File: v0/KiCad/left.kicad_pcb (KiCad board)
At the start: 2 copper layers, 153.3 x 124.9 mm, 3 parts

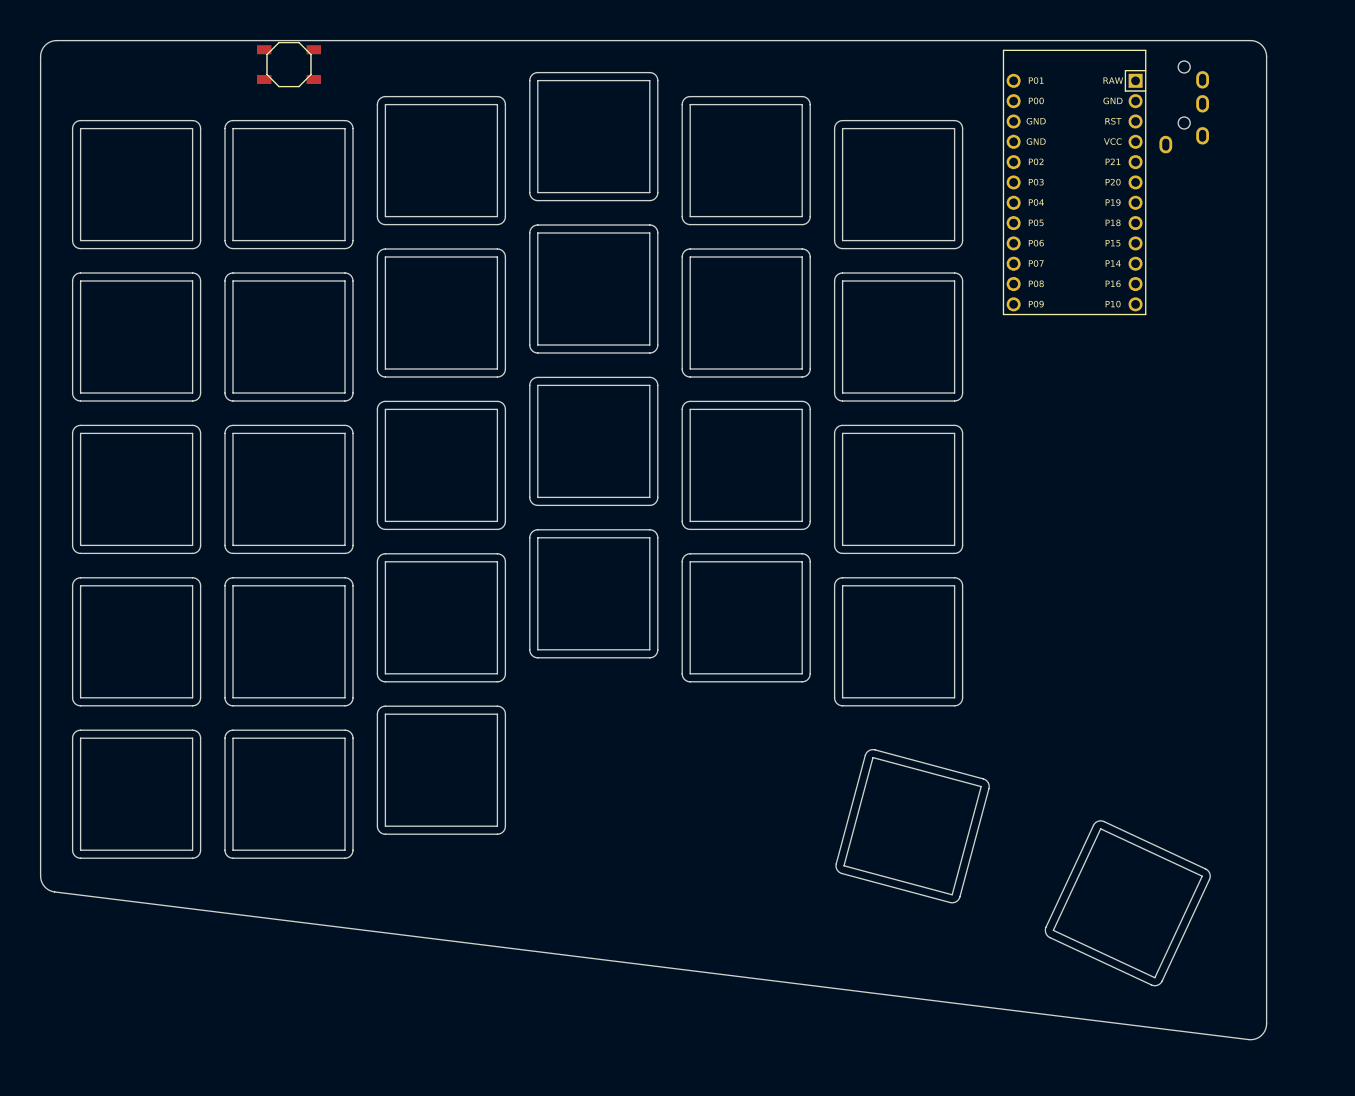
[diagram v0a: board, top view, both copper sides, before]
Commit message: Use 1.5u for mod
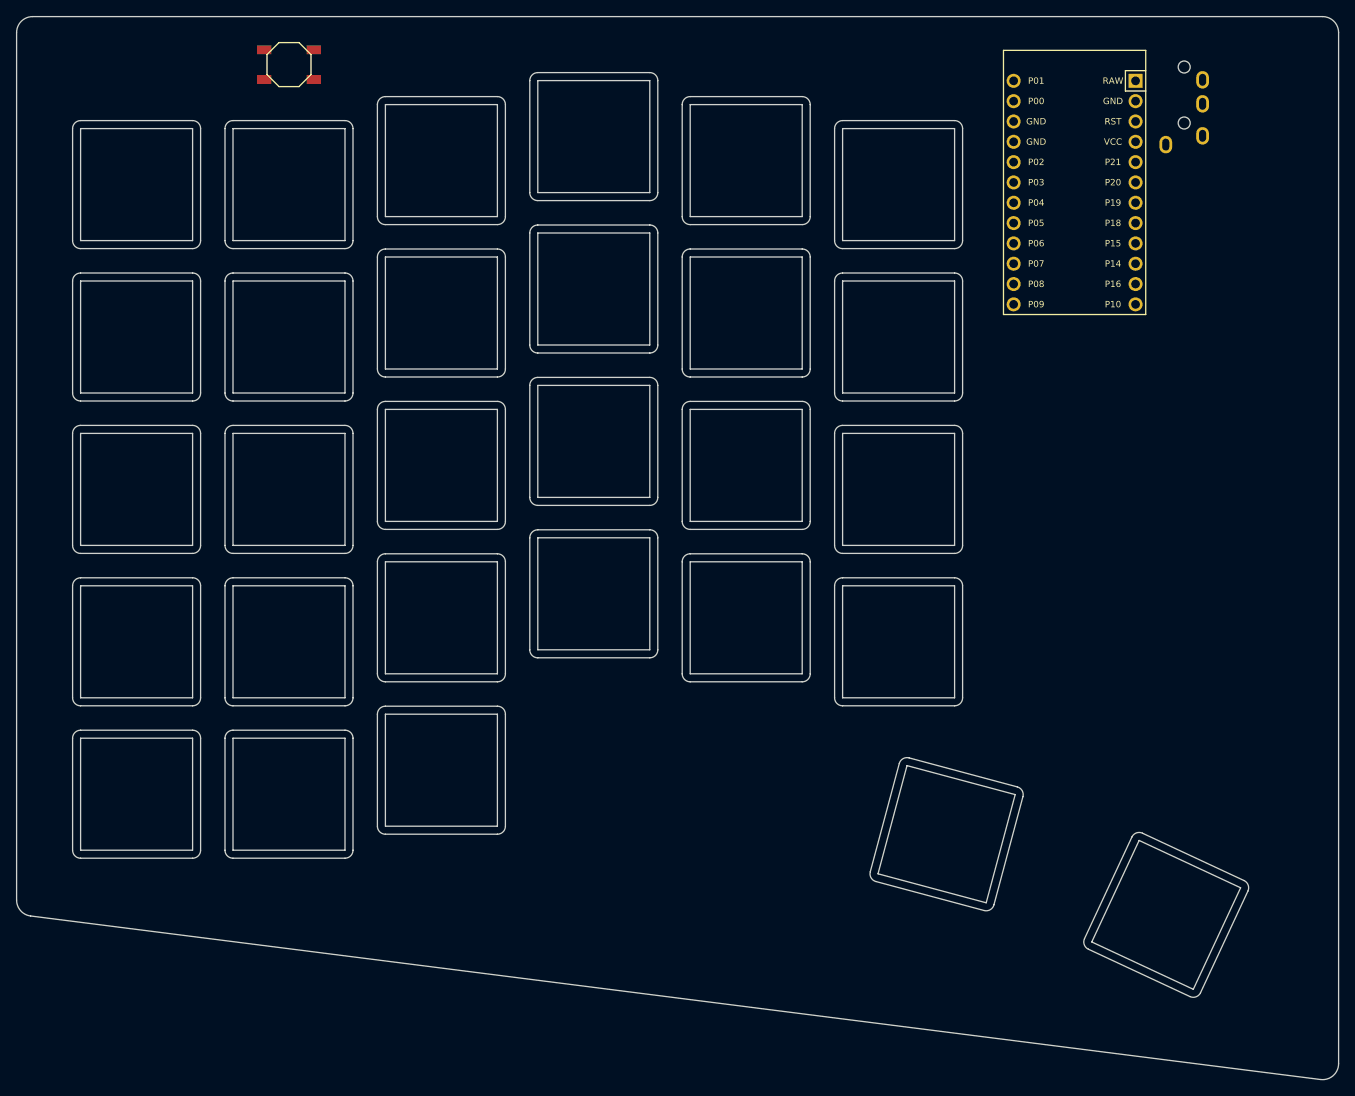
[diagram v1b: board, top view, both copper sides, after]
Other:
- board size 153.3 x 124.9 mm -> 165.2 x 132.9 mm
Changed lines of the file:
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@@
         (pad 4 thru_hole oval (at 0 3.2 0) (size 1.6 2.2) (drill oval 0.9 1.5) (layers *.Cu *.Mask) (net 4 "VCC"))
       )
-            (gr_line (start -12 10.23207596639478) (end -12 -92.2) (angle 90) (layer Edge.Cuts) (width 0.15))
-(gr_line (start -10 -94.2) (end 139.25 -94.2) (angle 90) (layer Edge.Cuts) (width 0.15))
-(gr_line (start 141.25 -92.2) (end 141.25 28.6874593269168) (angle 90) (layer Edge.Cuts) (width 0.15))
-(gr_line (start 139.00456100000002 30.672342126916806) (end -10.245439000000003 12.21695876639478) (angle 90) (layer Edge.Cuts) (width 0.15))
-(gr_arc (start -10 -92.2) (end -10 -94.2) (angle -90) (layer Edge.Cuts) (width 0.15))
-(gr_arc (start 139.25 -92.2) (end 141.25 -92.2) (angle -90) (layer Edge.Cuts) (width 0.15))
-(gr_arc (start 139.25 28.6874593269168) (end 139.004561 30.672342126916803) (angle -97.04907874949942) (layer Edge.Cuts) (width 0.15))
-(gr_arc (start -10 10.23207596639478) (end -12 10.23207596639478) (angle -82.95092125049979) (layer Edge.Cuts) (width 0.15))
+            (gr_line (start -15 13.237546751225413) (end -15 -95.2) (angle 90) (layer Edge.Cuts) (width 0.15))
+(gr_line (start -13 -97.2) (end 148.25 -97.2) (angle 90) (layer Edge.Cuts) (width 0.15))
+(gr_line (start 150.25 -95.2) (end 150.25 33.68043631249622) (angle 90) (layer Edge.Cuts) (width 0.15))
+(gr_line (start 147.99845820000002 35.66455491249623) (end -13.251541799999998 15.221665351225418) (angle 90) (layer Edge.Cuts) (width 0.15))
+(gr_arc (start -13 -95.2) (end -13 -97.2) (angle -90) (layer Edge.Cuts) (width 0.15))
+(gr_arc (start 148.25 -95.2) (end 150.25 -95.2) (angle -90) (layer Edge.Cuts) (width 0.15))
+(gr_arc (start 148.25 33.68043631249622) (end 147.9984582 35.66455491249622) (angle -97.22527654598952) (layer Edge.Cuts) (width 0.15))
+(gr_arc (start -13 13.237546751225413) (end -15 13.237546751225413) (angle -82.77472345401009) (layer Edge.Cuts) (width 0.15))
 (gr_line (start -7 8) (end 7 8) (angle 90) (layer Edge.Cuts) (width 0.15))
 (gr_line (start 8 7) (end 8 -7) (angle 90) (layer Edge.Cuts) (width 0.15))
@@
 (gr_line (start 102.25 -84.2) (end 88.25 -84.2) (angle 90) (layer Edge.Cuts) (width 0.15))
 (gr_line (start 87.25 -83.2) (end 87.25 -69.2) (angle 90) (layer Edge.Cuts) (width 0.15))
-(gr_line (start 88.1679668295753 9.915673251225952) (end 101.69092845122594 13.53913997042468) (angle 90) (layer Edge.Cuts) (width 0.15))
-(gr_line (start 102.91567325122595 12.832033170424609) (end 106.53913997042467 -0.6909284512259433) (angle 90) (layer Edge.Cuts) (width 0.15))
-(gr_line (start 105.83203317042468 -1.9156732512259538) (end 92.30907154877407 -5.539139970424678) (angle 90) (layer Edge.Cuts) (width 0.15))
-(gr_line (start 91.08432674877406 -4.8320331704246655) (end 87.46086002957531 8.690928451225943) (angle 90) (layer Edge.Cuts) (width 0.15))
-(gr_line (start 114.17361958611629 17.927815961854755) (end 126.86192856185481 23.844471613883755) (angle 90) (layer Edge.Cuts) (width 0.15))
-(gr_line (start 128.19085466185473 23.360782113883772) (end 134.10751031388372 10.672473138145278) (angle 90) (layer Edge.Cuts) (width 0.15))
-(gr_line (start 133.62382081388375 9.343547038145246) (end 120.93551183814522 3.426891386116253) (angle 90) (layer Edge.Cuts) (width 0.15))
-(gr_line (start 119.60658573814524 3.910580886116236) (end 113.68993008611625 16.598889861854758) (angle 90) (layer Edge.Cuts) (width 0.15))
-(gr_arc (start 127.28454686185478 22.938163813883747) (end 126.86192856185478 23.844471613883748) (angle -89.99999999999568) (layer Edge.Cuts) (width 0.15))
-(gr_arc (start 133.20120251388374 10.249854838145268) (end 134.10751031388375 10.672473138145268) (angle -90.00000000000098) (layer Edge.Cuts) (width 0.15))
-(gr_arc (start 120.51289353814522 4.333199186116261) (end 120.93551183814522 3.4268913861162607) (angle -89.99999999999784) (layer Edge.Cuts) (width 0.15))
-(gr_arc (start 114.59623788611627 17.02150816185477) (end 113.68993008611628 16.59888986185477) (angle -90.00000000000065) (layer Edge.Cuts) (width 0.15))
-(gr_arc (start 101.94974745122595 12.573214170424684) (end 101.69092845122594 13.539139970424685) (angle -90.00000000000455) (layer Edge.Cuts) (width 0.15))
-(gr_arc (start 105.57321417042468 -0.94974745122596) (end 106.53913997042467 -0.69092845122596) (angle -90.00000000000081) (layer Edge.Cuts) (width 0.15))
-(gr_arc (start 92.05025254877405 -4.573214170424677) (end 92.30907154877406 -5.539139970424677) (angle -90.00000000000149) (layer Edge.Cuts) (width 0.15))
-(gr_arc (start 88.42678582957532 8.949747451225903) (end 87.46086002957533 8.690928451225902) (angle -89.99999999999747) (layer Edge.Cuts) (width 0.15))
+(gr_line (start 92.4179668295753 10.915673251225952) (end 105.94092845122594 14.539139970424683) (angle 90) (layer Edge.Cuts) (width 0.15))
+(gr_line (start 107.16567325122594 13.832033170424666) (end 110.7891399704247 0.30907154877394305) (angle 90) (layer Edge.Cuts) (width 0.15))
+(gr_line (start 110.08203317042467 -0.9156732512259538) (end 96.55907154877401 -4.539139970424692) (angle 90) (layer Edge.Cuts) (width 0.15))
+(gr_line (start 95.33432674877405 -3.8320331704246655) (end 91.71086002957531 9.690928451225943) (angle 90) (layer Edge.Cuts) (width 0.15))
+(gr_line (start 118.97599198611624 19.37627636185475) (end 131.6643009618547 25.29293201388372) (angle 90) (layer Edge.Cuts) (width 0.15))
+(gr_line (start 132.99322706185475 24.809242513883703) (end 138.9098827138837 12.120933538145266) (angle 90) (layer Edge.Cuts) (width 0.15))
+(gr_line (start 138.42619321388366 10.79200743814522) (end 125.7378842381452 4.875351786116241) (angle 90) (layer Edge.Cuts) (width 0.15))
+(gr_line (start 124.40895813814525 5.3590412861162235) (end 118.49230248611623 18.04735026185483) (angle 90) (layer Edge.Cuts) (width 0.15))
+(gr_arc (start 132.08691926185472 24.386624213883735) (end 131.6643009618547 25.292932013883735) (angle -90.0000000000035) (layer Edge.Cuts) (width 0.15))
+(gr_arc (start 138.00357491388368 11.698315238145256) (end 138.9098827138837 12.120933538145255) (angle -90.00000000000219) (layer Edge.Cuts) (width 0.15))
+(gr_arc (start 125.31526593814522 5.781659586116255) (end 125.73788423814521 4.875351786116255) (angle -89.99999999999619) (layer Edge.Cuts) (width 0.15))
+(gr_arc (start 119.39861028611624 18.469968561854785) (end 118.49230248611624 18.047350261854785) (angle -89.99999999999673) (layer Edge.Cuts) (width 0.15))
+(gr_arc (start 106.19974745122595 13.573214170424684) (end 105.94092845122594 14.539139970424685) (angle -90.00000000000108) (layer Edge.Cuts) (width 0.15))
+(gr_arc (start 109.82321417042469 0.05025254877398311) (end 110.78913997042469 0.30907154877398313) (angle -89.99999999999818) (layer Edge.Cuts) (width 0.15))
+(gr_arc (start 96.30025254877404 -3.5732141704246843) (end 96.55907154877404 -4.539139970424684) (angle -89.9999999999994) (layer Edge.Cuts) (width 0.15))
+(gr_arc (start 92.67678582957531 9.94974745122596) (end 91.71086002957531 9.69092845122596) (angle -90.00000000000082) (layer Edge.Cuts) (width 0.15))
 (gr_arc (start 64.15 -37.1) (end 64.15 -36.1) (angle -90) (layer Edge.Cuts) (width 0.15))
 (gr_arc (start 64.15 -51.1) (end 65.15 -51.1) (angle -90) (layer Edge.Cuts) (width 0.15))
@@
 (gr_line (start 102.25 -83.2) (end 88.25 -83.2) (angle 90) (layer Edge.Cuts) (width 0.15))
 (gr_line (start 88.25 -83.2) (end 88.25 -69.2) (angle 90) (layer Edge.Cuts) (width 0.15))
-(gr_line (start 88.4267859 8.9497475) (end 101.9497475 12.5732141) (angle 90) (layer Edge.Cuts) (width 0.15))
-(gr_line (start 101.9497475 12.5732141) (end 105.5732141 -0.9497475000000009) (angle 90) (layer Edge.Cuts) (width 0.15))
-(gr_line (start 105.5732141 -0.9497475000000009) (end 92.0502525 -4.5732140999999995) (angle 90) (layer Edge.Cuts) (width 0.15))
-(gr_line (start 92.0502525 -4.5732140999999995) (end 88.4267859 8.9497475) (angle 90) (layer Edge.Cuts) (width 0.15))
-(gr_line (start 114.5962379 17.021508199999996) (end 127.2845469 22.938163799999998) (angle 90) (layer Edge.Cuts) (width 0.15))
-(gr_line (start 127.2845469 22.938163799999998) (end 133.2012025 10.249854799999998) (angle 90) (layer Edge.Cuts) (width 0.15))
-(gr_line (start 133.2012025 10.249854799999998) (end 120.5128935 4.333199199999996) (angle 90) (layer Edge.Cuts) (width 0.15))
-(gr_line (start 120.5128935 4.333199199999996) (end 114.5962379 17.021508199999996) (angle 90) (layer Edge.Cuts) (width 0.15))
+(gr_line (start 92.6767859 9.9497475) (end 106.1997475 13.5732141) (angle 90) (layer Edge.Cuts) (width 0.15))
+(gr_line (start 106.1997475 13.5732141) (end 109.8232141 0.050252499999999145) (angle 90) (layer Edge.Cuts) (width 0.15))
+(gr_line (start 109.8232141 0.050252499999999145) (end 96.3002525 -3.5732140999999995) (angle 90) (layer Edge.Cuts) (width 0.15))
+(gr_line (start 96.3002525 -3.5732140999999995) (end 92.6767859 9.9497475) (angle 90) (layer Edge.Cuts) (width 0.15))
+(gr_line (start 119.39861029999999 18.469968599999998) (end 132.08691929999998 24.3866242) (angle 90) (layer Edge.Cuts) (width 0.15))
+(gr_line (start 132.08691929999998 24.3866242) (end 138.0035749 11.6983152) (angle 90) (layer Edge.Cuts) (width 0.15))
+(gr_line (start 138.0035749 11.6983152) (end 125.31526589999999 5.781659599999998) (angle 90) (layer Edge.Cuts) (width 0.15))
+(gr_line (start 125.31526589999999 5.781659599999998) (end 119.39861029999999 18.469968599999998) (angle 90) (layer Edge.Cuts) (width 0.15))
 )
